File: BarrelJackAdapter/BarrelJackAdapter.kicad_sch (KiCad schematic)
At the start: 6 parts, among them J1 Barrel_Jack_Switch, J2 Conn_01x03, J4 Conn_01x03, U1 L7805

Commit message: working on an SMD version of the little adapter
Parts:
- C1, C2: footprint Capacitor_SMD:C_0201_0603Metric -> Capacitor_SMD:C_0603_1608Metric
- U1: footprint Package_TO_SOT_THT:TO-220-3_Vertical -> Package_TO_SOT_SMD:TO-263-2
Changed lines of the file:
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@@
 			)
 		)
-		(property "Footprint" "Package_TO_SOT_THT:TO-220-3_Vertical"
+		(property "Footprint" "Package_TO_SOT_SMD:TO-263-2"
 			(at 128.905 66.04 0)
 			(effects
@@
 			)
 		)
-		(property "Footprint" "Capacitor_SMD:C_0201_0603Metric"
+		(property "Footprint" "Capacitor_SMD:C_0603_1608Metric"
 			(at 140.97 68.58 0)
 			(effects
@@
 			)
 		)
-		(property "Footprint" "Capacitor_SMD:C_0201_0603Metric"
+		(property "Footprint" "Capacitor_SMD:C_0603_1608Metric"
 			(at 113.03 68.58 0)
 			(effects

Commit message: wip
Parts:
- removed C1: 0.33u, Capacitor_SMD:C_0603_1608Metric, symbol Device:C_Small
- removed C2: 0.1u, Capacitor_SMD:C_0603_1608Metric, symbol Device:C_Small
- removed U1: L7805, Package_TO_SOT_SMD:TO-263-2, symbol Regulator_Linear:L7805
- added C1: C_10U_805, Capacitor_SMD:C_0805_2012Metric, symbol StockedComponents:C_10U_805
- added C2, C3: C_P1U, Capacitor_SMD:C_0603_1608Metric, symbol StockedComponents:C_P1U
- added C4, C5: C_22U_1210, Capacitor_SMD:C_1210_3225Metric, symbol StockedComponents:C_22U_1210
- added L1: L_4p7U_13p5A, Inductor_SMD:L_Coilcraft_XxL4040, symbol StockedComponents:L_4p7U_13p5A
- added R1: R_49p9K, Resistor_SMD:R_0603_1608Metric, symbol StockedComponents:R_49p9K
- added R2: R_10K, Resistor_SMD:R_0603_1608Metric, symbol StockedComponents:R_10K
- added U1: TPS563207DRLR, Package_TO_SOT_SMD:SOT-563, symbol StockedComponents:TPS563207DRLR
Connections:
- net +5V: now also C4.1, C5.1, L1.2, R1.1
- net +9V: now also C1.1, C2.1, U1.1 (VIN), U1.5 (EN)
- net GND: now also C1.2, C2.2, C4.2, C5.2, R2.2, U1.3 (GND)
- new net: R1.2, R2.1, U1.6 (FB)
- new net: C3.1, L1.1, U1.4 (BST)
- new net: C3.2, U1.2 (SW)
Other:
- moved on the sheet: J1

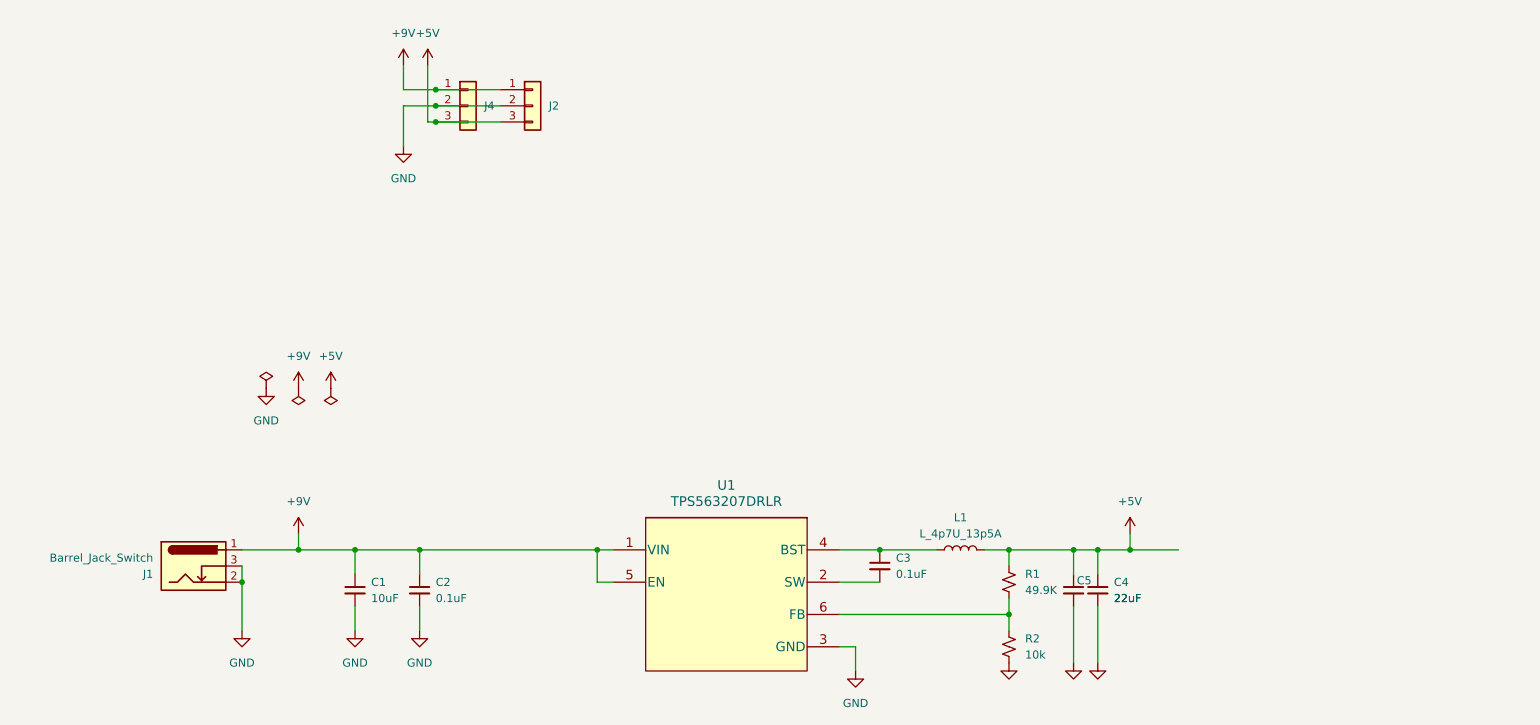
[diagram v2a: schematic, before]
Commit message: add 3.3v LDO
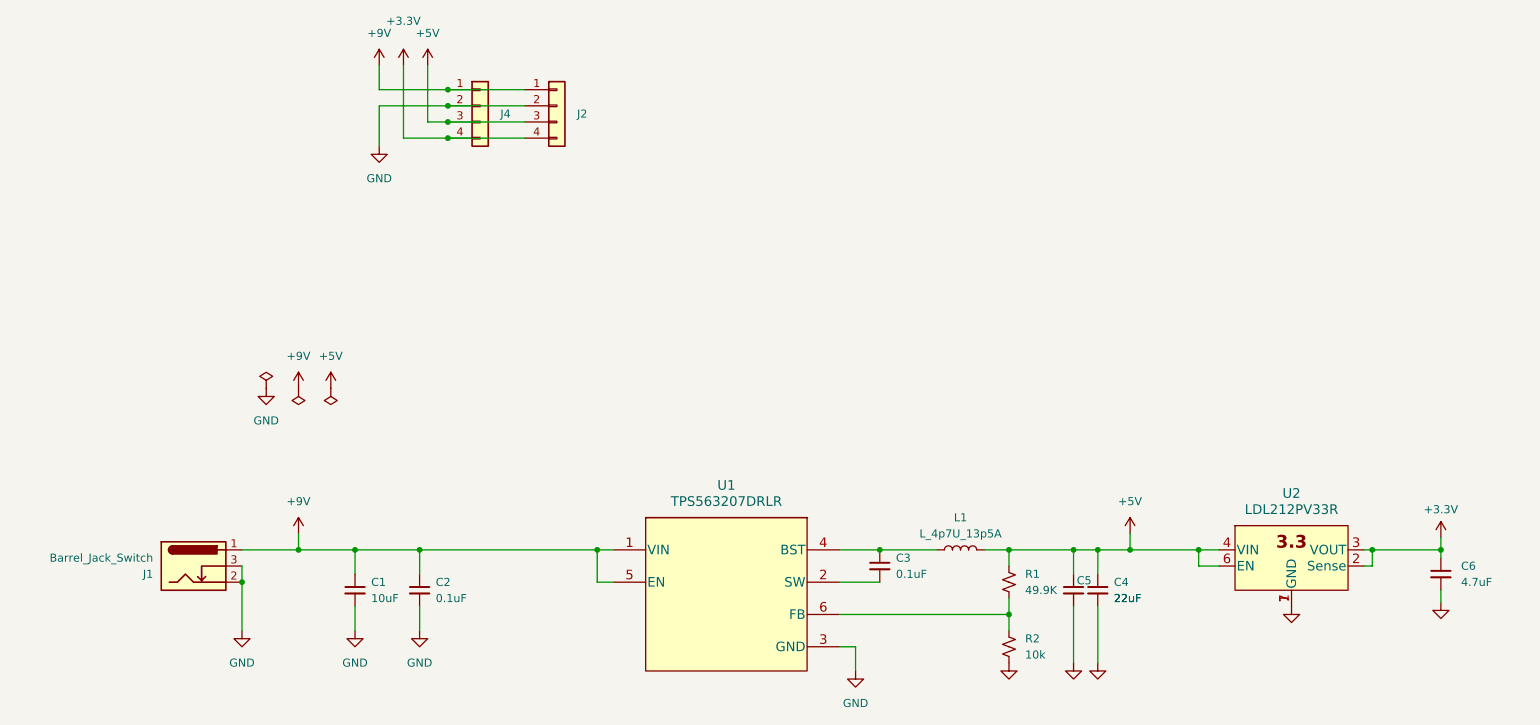
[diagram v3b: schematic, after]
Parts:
- removed J2, J4: Conn_01x03, Connector_PinHeader_2.54mm:PinHeader_1x03_P2.54mm_Vertical, symbol Connector_Generic:Conn_01x03
- added C6: C_4p7U, Capacitor_SMD:C_0603_1608Metric, symbol StockedComponents:C_4p7U
- added J2, J4: Conn_01x04, Connector_PinHeader_2.54mm:PinHeader_1x04_P2.54mm_Vertical, symbol Connector_Generic:Conn_01x04
- added U2: LDL212PV33R, Package_DFN_QFN:DFN-6-1EP_2x2mm_P0.65mm_EP1x1.6mm, symbol StockedComponents:LDL212PV33R
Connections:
- net +5V: now also J2.3 (Pin_3), J4.3 (Pin_3), U2.4 (VIN), U2.6 (EN)
- net +9V: now also J2.1 (Pin_1), J4.1 (Pin_1)
- net GND: now also C6.2, J2.2 (Pin_2), J4.2 (Pin_2), U2.1 (GND), U2.7 (GND)
- new net +3.3V: C6.1, J2.4 (Pin_4), J4.4 (Pin_4), U2.2 (Sense), U2.3 (VOUT)

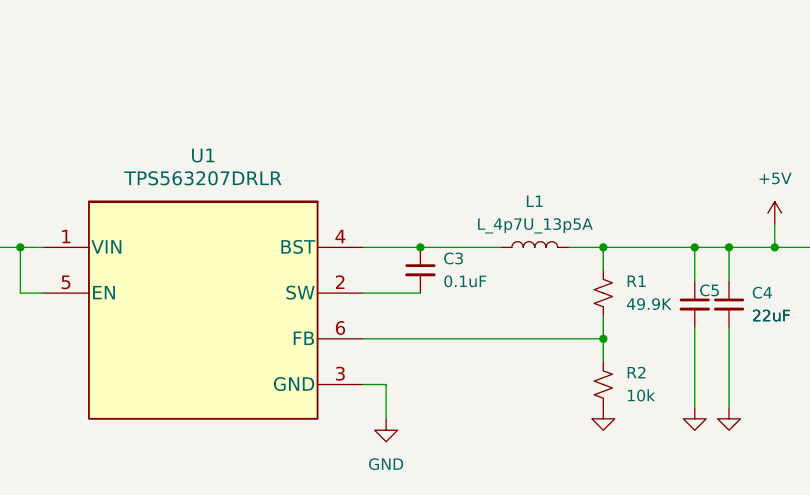
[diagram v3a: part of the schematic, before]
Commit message: Remove some vias to the back ground plane.
Localize the high current loop to Front Copper.

Move the switch node connection to Cu2 - sandwich
between clean ground pours.
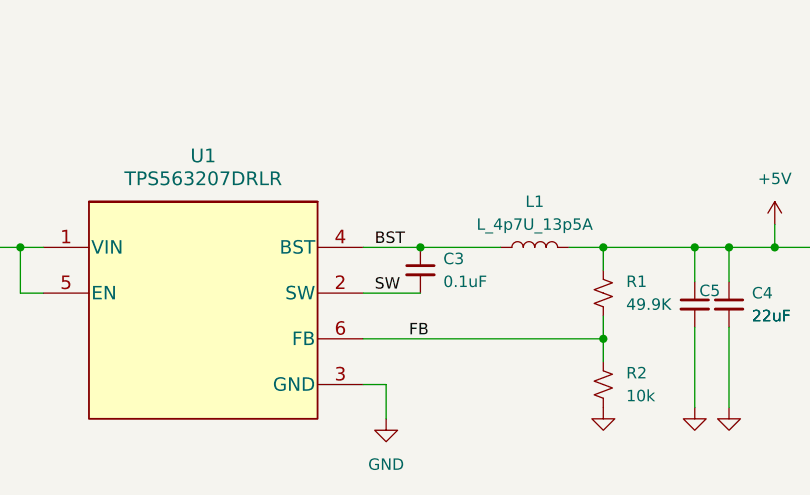
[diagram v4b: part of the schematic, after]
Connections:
- net FB: now reaches R1.2, R2.1, U1.6 (FB)
- net BST: now reaches C3.1, L1.1, U1.4 (BST)
- net SW: now reaches C3.2, U1.2 (SW)
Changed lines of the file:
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@@
+		)
+	)
+	(label "BST"
+		(at 166.37 109.22 0)
+		(fields_autoplaced yes)
+		(effects
+			(font
+				(size 1.27 1.27)
+			)
+			(justify left bottom)
+		)
+	)
+	(label "FB"
+		(at 170.18 119.38 0)
+		(fields_autoplaced yes)
+		(effects
+			(font
+				(size 1.27 1.27)
+			)
+			(justify left bottom)
+		)
+	)
+	(label "SW"
+		(at 166.37 114.3 0)
+		(fields_autoplaced yes)
+		(effects
+			(font
+				(size 1.27 1.27)
+			)
+			(justify left bottom)
 		)
 	)

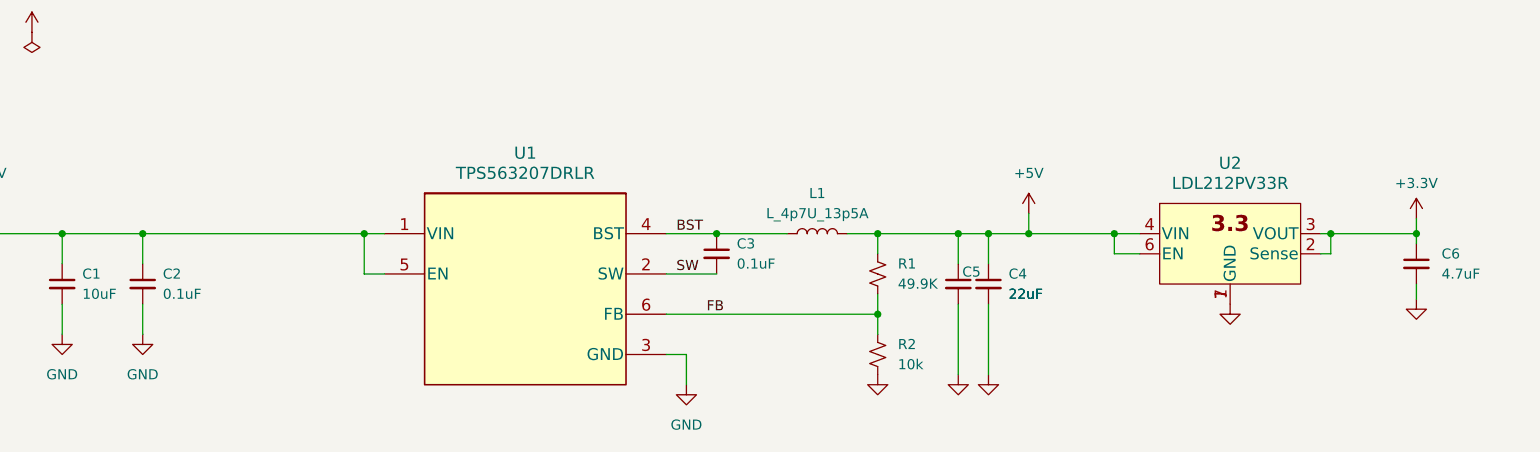
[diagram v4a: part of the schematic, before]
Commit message: Fix schematic.
Better Layout

Close #2
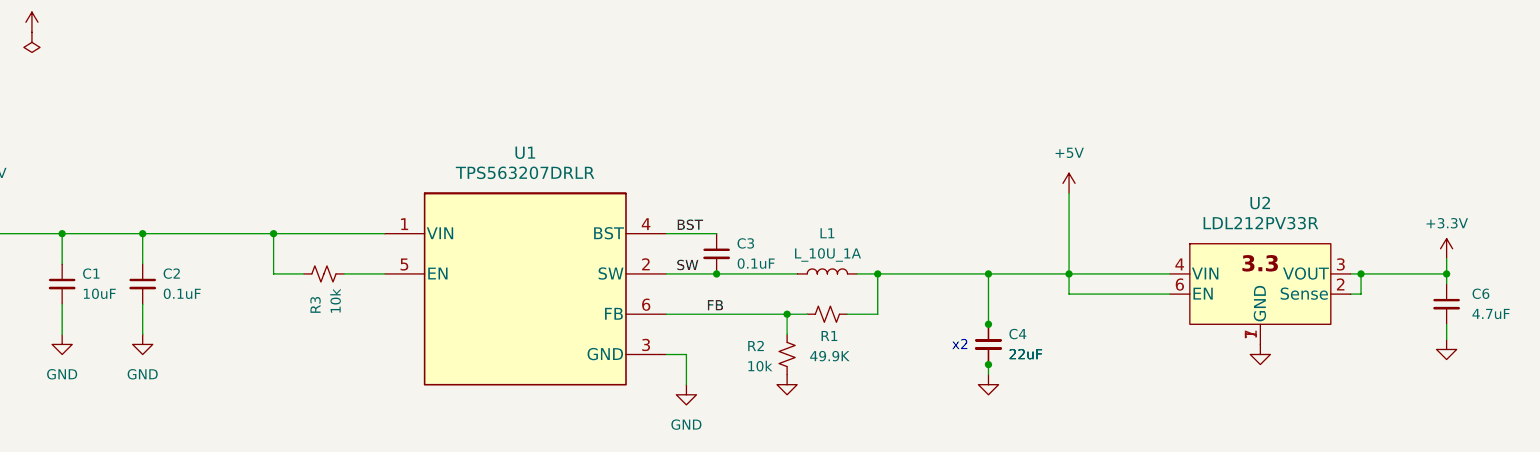
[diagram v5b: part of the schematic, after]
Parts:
- removed C5: C_22U_1210, Capacitor_SMD:C_1210_3225Metric, symbol StockedComponents:C_22U_1210
- added C7: C_22U_1210, Capacitor_SMD:C_1210_3225Metric, symbol StockedComponents:C_22U_1210
- added R3: R_10K, Resistor_SMD:R_0603_1608Metric, symbol StockedComponents:R_10K
- L1: value L_4p7U_13p5A -> L_10U_1A; symbol StockedComponents:L_4p7U_13p5A -> StockedComponents:L_10U_1A
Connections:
- net +5V: now also C7.1
- net +9V: now also R3.1; no longer U1.5 (EN)
- net BST: no longer L1.1
- net GND: now also C7.2
- net SW: now also L1.1
- new net: R3.2, U1.5 (EN)
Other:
- note added: "x2"
- moved on the sheet: C4, C6, L1, R1, R2, U2

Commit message: Work on BOM.
Be very skeptical of this checkin.  There were some merge shenanigans involved.
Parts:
- J1: DigiKey PN (none) -> CP-102AH-ND
- L1: DigiKey PN (none) -> 2457-XGL4040-103MEC-ND
- U2: DigiKey PN (none) -> 497-19548-2-ND
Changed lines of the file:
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@@
 (kicad_sch
-	(version 20231120)
+	(version 20250114)
 	(generator "eeschema")
-	(generator_version "8.0")
+	(generator_version "9.0")
 	(paper "A4")
+	(text "x2"
+		(exclude_from_sim no)
+		(at 202.184 123.444 0)
+		(effects
+			(font
+				(size 1.27 1.27)
+			)
+		)
+	)
 	(junction
 		(at 215.9 114.3)
@@
 		)
 	)
-	(text "x2"
-		(exclude_from_sim no)
-		(at 202.184 123.444 0)
-		(effects
-			(font
-				(size 1.27 1.27)
-			)
-		)
-	)
 	(label "BST"
 		(at 166.37 109.22 0)
-		(fields_autoplaced yes)
 		(effects
 			(font
@@
 	(label "FB"
 		(at 170.18 119.38 0)
-		(fields_autoplaced yes)
 		(effects
 			(font
@@
 	(label "SW"
 		(at 166.37 114.3 0)
-		(fields_autoplaced yes)
 		(effects
 			(font
@@
 			)
 		)
+		(property "DigiKey PN" "2457-XGL4040-103MEC-ND"
+			(at 185.42 114.3 0)
+			(effects
+				(font
+					(size 1.27 1.27)
+				)
+			)
+		)
 		(pin "2"
 		)
@@
 			)
 		)
+		(property "DigiKey PN" "CP-102AH-ND"
+			(at 63.5 111.76 0)
+			(effects
+				(font
+					(size 1.27 1.27)
+				)
+			)
+		)
 		(pin "3"
 		)
@@
 			)
 		)
+		(property "DigiKey PN" "497-19548-2-ND"
+			(at 223.52 115.57 0)
+			(effects
+				(font
+					(size 1.27 1.27)
+				)
+			)
+		)
 		(pin "3"
 		)
@@
 		)
 	)
+	(embedded_fonts no)
 )
